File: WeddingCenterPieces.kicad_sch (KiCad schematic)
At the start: 24 parts, among them J1 Batt_In, J2 WS2812, J3 Btn_OffBoard, SW1 Btn_OnBoard, U1 Pico, U2 TXS0101DBV, U3 MC33063AP

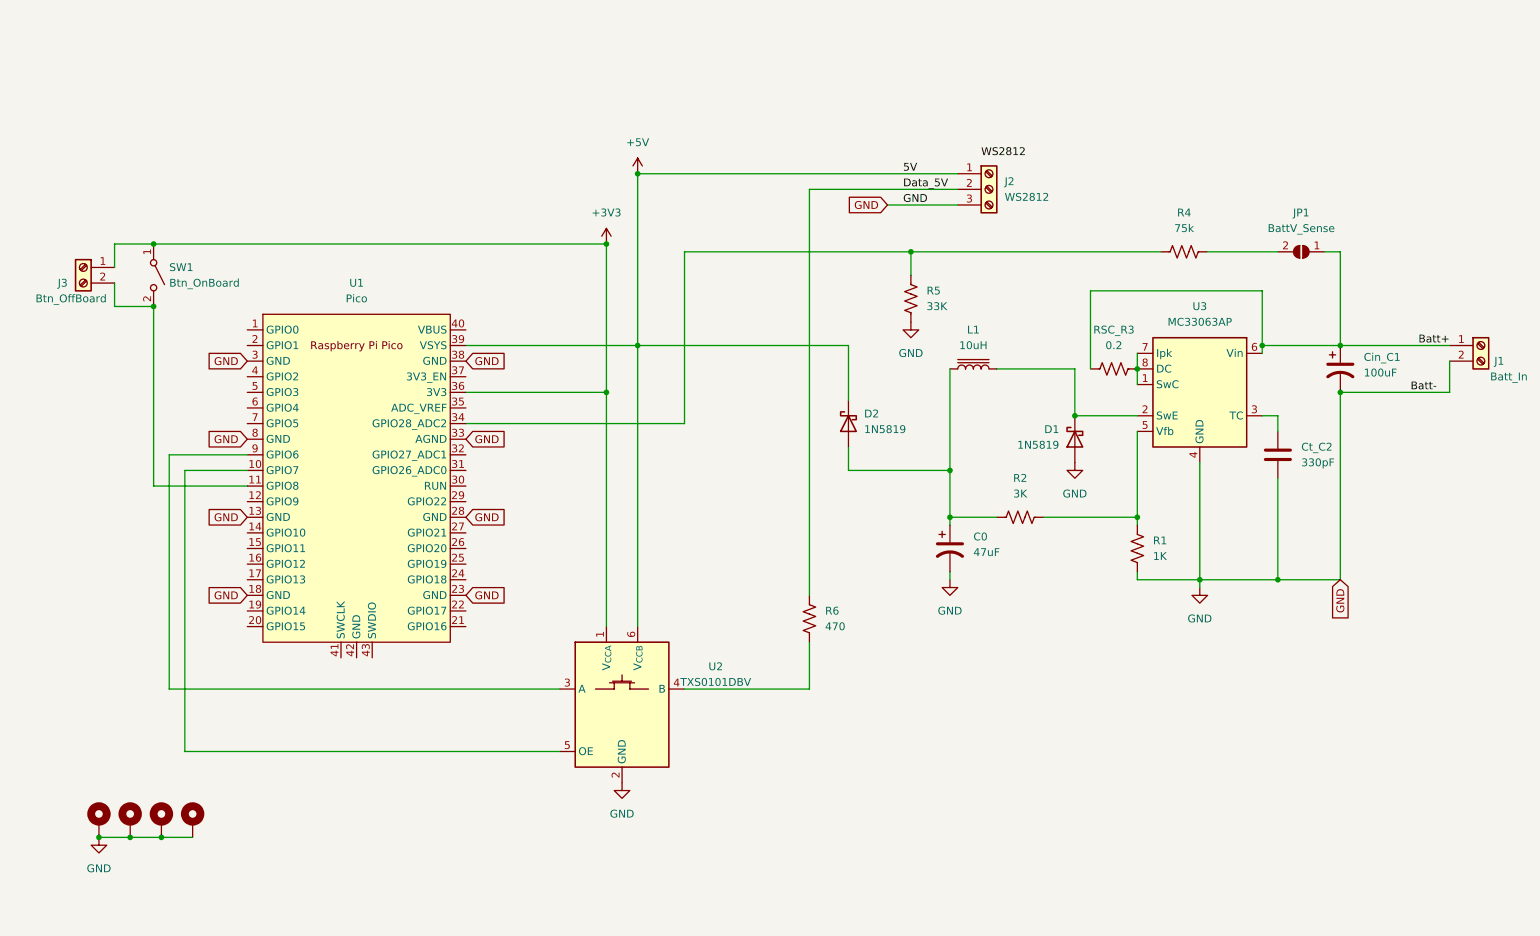
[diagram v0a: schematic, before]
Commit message: Pulling out Power Supply into a separate sheet.
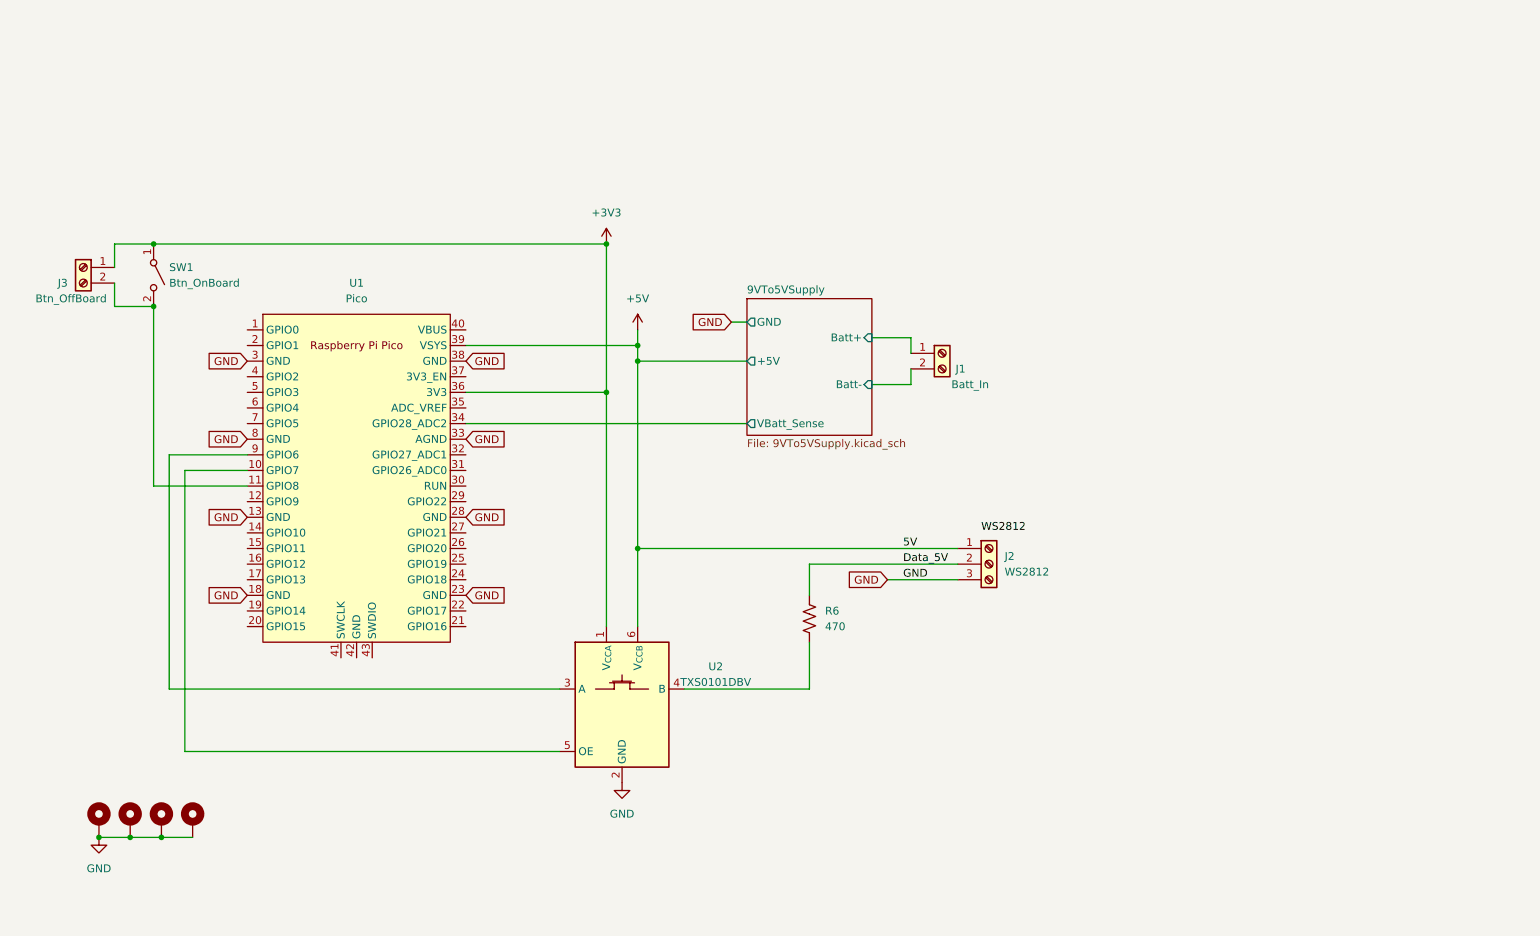
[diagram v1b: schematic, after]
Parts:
- removed C0: 47uF, Capacitor_THT:CP_Radial_D5.0mm_P2.00mm, symbol Device:C_Polarized_US
- removed Cin_C1: 100uF, Capacitor_THT:CP_Radial_D5.0mm_P2.00mm, symbol Device:C_Polarized_US
- removed Ct_C2: 330pF, Capacitor_THT:C_Disc_D3.0mm_W1.6mm_P2.50mm, symbol Device:C
- removed D1, D2: 1N5819, Diode_THT:D_DO-41_SOD81_P10.16mm_Horizontal, symbol Diode:1N5819
- removed JP1: BattV_Sense, Jumper:SolderJumper-2_P1.3mm_Open_TrianglePad1.0x1.5mm, symbol Jumper:SolderJumper_2_Open
- removed L1: 10uH, Inductor_THT:L_Radial_D8.7mm_P5.00mm_Fastron_07HCP, symbol Device:L_Iron
- removed R1: 1K, Resistor_THT:R_Axial_DIN0207_L6.3mm_D2.5mm_P7.62mm_Horizontal, symbol Device:R_US
- removed R2: 3K, Resistor_THT:R_Axial_DIN0207_L6.3mm_D2.5mm_P7.62mm_Horizontal, symbol Device:R_US
- removed R4: 75k, Resistor_THT:R_Axial_DIN0309_L9.0mm_D3.2mm_P12.70mm_Horizontal, symbol Device:R_US
- removed R5: 33K, Resistor_THT:R_Axial_DIN0204_L3.6mm_D1.6mm_P5.08mm_Horizontal, symbol Device:R_US
- removed RSC_R3: 0.2, Resistor_THT:R_Axial_DIN0414_L11.9mm_D4.5mm_P15.24mm_Horizontal, symbol Device:R_US
- removed U3: MC33063AP, Package_DIP:DIP-8_W7.62mm, symbol Regulator_Switching:MC33063AP
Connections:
- net GND: no longer J1.2 (Pin_2)
- net 9VTo5VSupply/VBatt_Sense: now reaches U1.34 (GPIO28_ADC2)
- net Batt+ renamed 9VTo5VSupply/Batt+
- new net 9VTo5VSupply/Batt-: J1.2 (Pin_2)
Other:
- added sheet 9VTo5VSupply (9VTo5VSupply.kicad_sch)
- moved on the sheet: J1, J2

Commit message: WIP: Updating board to use an RP2040 directly.
TODO: Need to update on-board LEDs to SK6812 Mini-E, fix VSYS/VBUS/+5V, and convert any footprints of interest to SMD
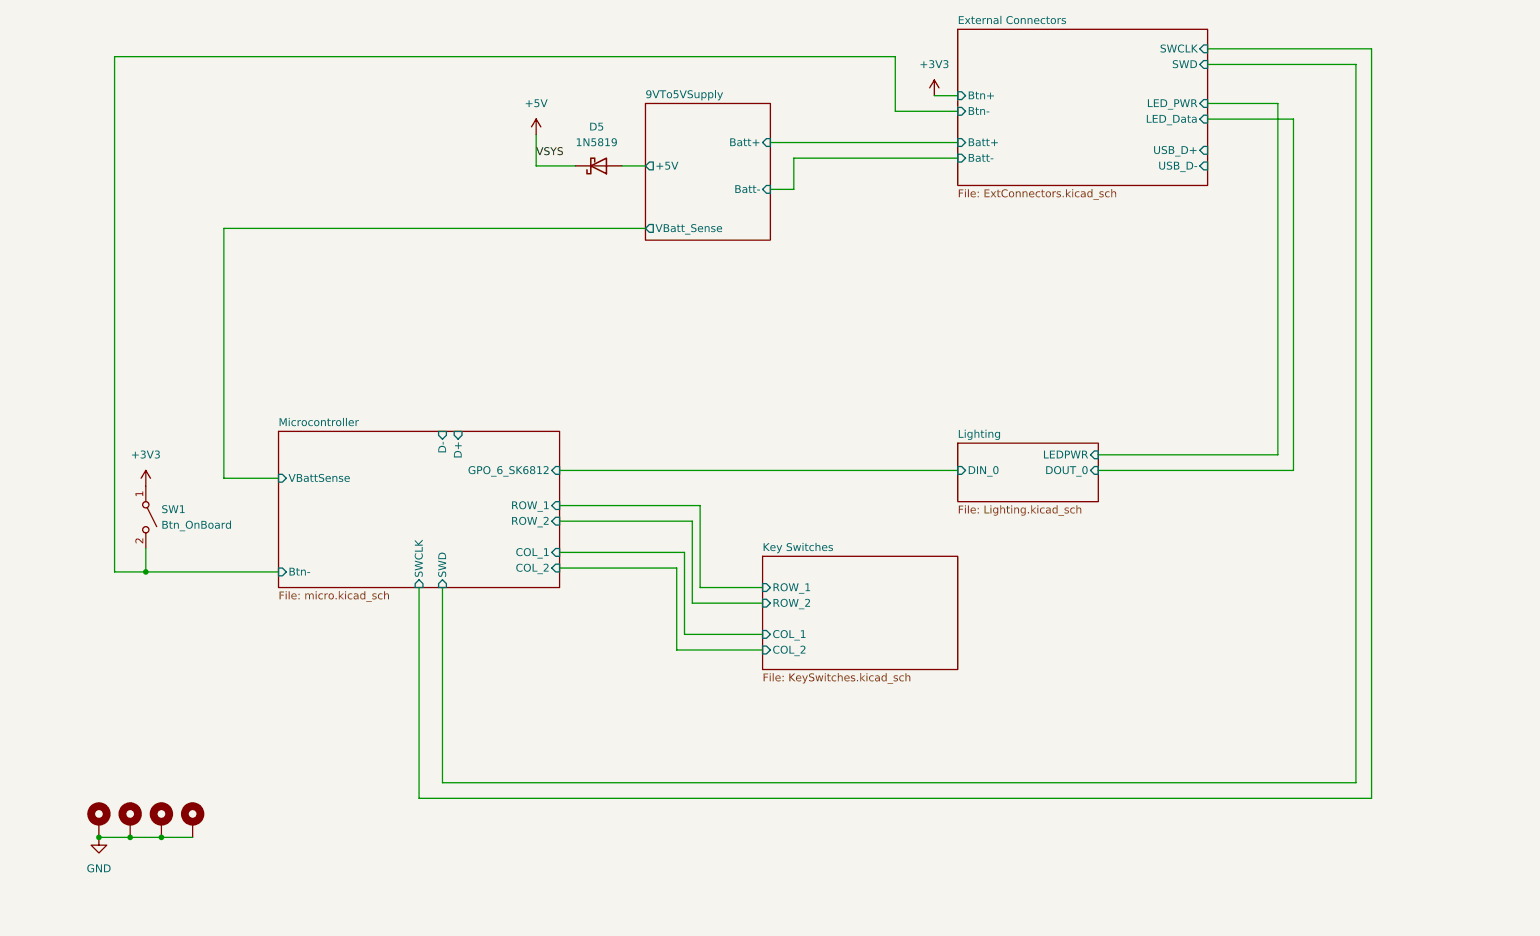
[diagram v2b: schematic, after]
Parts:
- removed J1: Batt_In, TerminalBlock:TerminalBlock_Altech_AK300-2_P5.00mm, symbol Connector:Screw_Terminal_01x02
- removed J2: WS2812, TerminalBlock:TerminalBlock_Altech_AK300-3_P5.00mm, symbol Connector:Screw_Terminal_01x03
- removed J3: Btn_OffBoard, TerminalBlock:TerminalBlock_Altech_AK300-2_P5.00mm, symbol Connector:Screw_Terminal_01x02
- removed R6: 470, Resistor_THT:R_Axial_DIN0207_L6.3mm_D2.5mm_P7.62mm_Horizontal, symbol Device:R_US
- removed U1: Pico, MCU_RaspberryPi_and_Boards:RPi_Pico_SMD_TH, symbol MCU_RaspberryPi_and_Boards:Pico
- removed U2: TXS0101DBV, Package_TO_SOT_SMD:SOT-23-6, symbol Logic_LevelTranslator:TXS0101DBV
- added D5: 1N5819, Diode_THT:D_DO-41_SOD81_P10.16mm_Horizontal, symbol Diode:1N5819
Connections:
- net +5V: now also D5.1 (K)
- net External Connectors/Btn-: now reaches SW1.2 (B)
- new net 9VTo5VSupply/+5V: D5.2 (A)
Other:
- added sheet External Connectors (ExtConnectors.kicad_sch)
- added sheet Key Switches (KeySwitches.kicad_sch)
- added sheet Lighting (Lighting.kicad_sch)
- added sheet Microcontroller (micro.kicad_sch)
- sheet 9VTo5VSupply ports: added none; removed GND
- moved on the sheet: SW1

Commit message: Placing nearly all components onto the PCB. Removing the 9Vto5V battery input stage from populating onto the PCB.
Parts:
- removed H1, H2, H3, H4: MountingHole_Pad, MountingHole:MountingHole_2.7mm_M2.5_Pad, symbol Mechanical:MountingHole_Pad
- added H1, H2, H3, H4: MountingHole, MountingHole:MountingHole_2.7mm_M2.5, symbol Mechanical:MountingHole

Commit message: Adding additional LEDs and driver to test per-key LEDs, updating net classes and design constraints, and starting to route tracks.
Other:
- sheet Lighting ports: added DIN_1; removed none
- sheet Microcontroller ports: added GPO_7_SK6812; removed none
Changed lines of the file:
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@@
+	(wire
+		(pts
+			(xy 120.65 104.14) (xy 185.42 104.14)
+		)
+		(stroke
+			(width 0)
+			(type default)
+		)
+	)
 	(wire
 		(pts
@@
 			)
 		)
+		(pin "DIN_1" input
+			(at 185.42 104.14 180)
+			(effects
+				(font
+					(size 1.27 1.27)
+				)
+				(justify left)
+			)
+		)
 		(instances
 			(project "WeddingCenterPieces"
@@
 			(effects
 				(font
+					(size 1.27 1.27)
+				)
+				(justify right)
+			)
+		)
+		(pin "GPO_7_SK6812" input
+			(at 120.65 104.14 0)
+			(effects
+				(font

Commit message: Shrinking board to only have 2 key switches and a few other unnecessary components. Finished with routing the rest of the board.
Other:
- sheet Key Switches ports: added none; removed COL_2
- sheet Lighting ports: added none; removed DIN_1
- sheet Microcontroller ports: added none; removed COL_2, GPO_7_SK6812
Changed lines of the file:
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@@
-	(wire
-		(pts
-			(xy 139.7 117.475) (xy 120.65 117.475)
-		)
-		(stroke
-			(width 0)
-			(type default)
-		)
-	)
 	(wire
 		(pts
@@
 	(wire
 		(pts
-			(xy 139.7 130.81) (xy 153.67 130.81)
-		)
-		(stroke
-			(width 0)
-			(type default)
-		)
-	)
-	(wire
-		(pts
 			(xy 154.94 48.26) (xy 185.42 48.26)
 		)
@@
 	(wire
 		(pts
-			(xy 139.7 130.81) (xy 139.7 117.475)
-		)
-		(stroke
-			(width 0)
-			(type default)
-		)
-	)
-	(wire
-		(pts
 			(xy 237.49 99.06) (xy 237.49 41.91)
 		)
@@
 		(pts
 			(xy 130.81 52.07) (xy 134.62 52.07)
-		)
-		(stroke
-			(width 0)
-			(type default)
-		)
-	)
-	(wire
-		(pts
-			(xy 120.65 104.14) (xy 185.42 104.14)
 		)
 		(stroke
@@
 		(exclude_from_sim no)
 		(in_bom yes)
-		(on_board yes)
+		(on_board no)
 		(dnp no)
 		(fields_autoplaced yes)
@@
 			)
 		)
-		(pin "COL_2" input
-			(at 153.67 130.81 180)
-			(effects
-				(font
-					(size 1.27 1.27)
-				)
-				(justify left)
-			)
-		)
 		(pin "ROW_1" input
 			(at 153.67 120.65 180)
@@
 			)
 		)
-		(pin "DIN_1" input
-			(at 185.42 104.14 180)
-			(effects
-				(font
-					(size 1.27 1.27)
-				)
-				(justify left)
-			)
-		)
 		(instances
 			(project "WeddingCenterPieces"
@@
 			)
 		)
-		(pin "COL_2" input
-			(at 120.65 117.475 0)
-			(effects
-				(font
-					(size 1.27 1.27)
-				)
-				(justify right)
-			)
-		)
 		(pin "ROW_1" input
 			(at 120.65 107.315 0)
@@
 			(effects
 				(font
-					(size 1.27 1.27)
-				)
-				(justify right)
-			)
-		)
-		(pin "GPO_7_SK6812" input
-			(at 120.65 104.14 0)
-			(effects
-				(font
